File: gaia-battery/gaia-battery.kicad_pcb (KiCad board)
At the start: 2 copper layers, 50 x 50 mm, 3 parts, among them J1 Conn_02x10_Odd_Even, J2 Conn_02x10_Odd_Even, J3 Conn_01x02_Pin

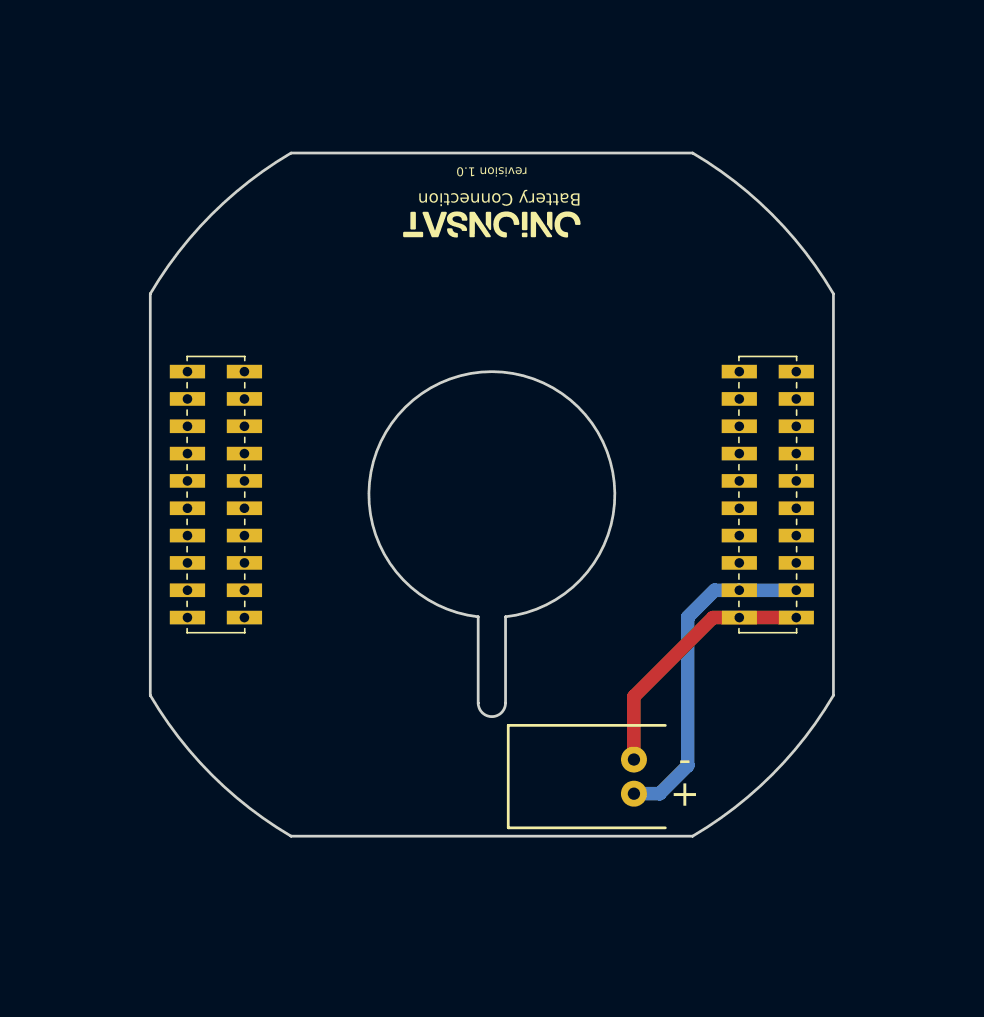
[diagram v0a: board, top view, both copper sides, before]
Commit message: fixing routing problems
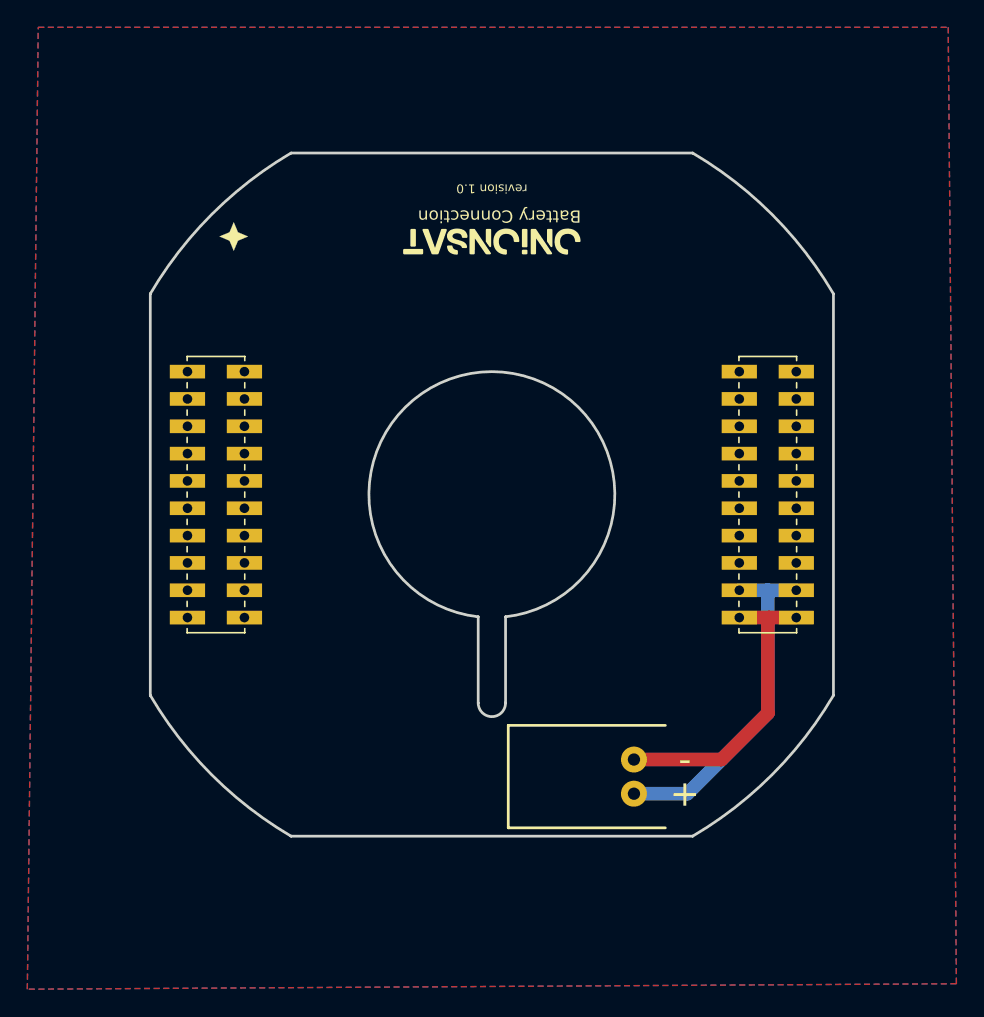
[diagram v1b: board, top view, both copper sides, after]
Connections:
- J1 pad 17: unconnected-(J1-Pin_17-Pad17) -> GND
- J1 pad 18: unconnected-(J1-Pin_18-Pad18) -> GND
- J1 pad 19: unconnected-(J1-Pin_19-Pad19) -> GND
- J1 pad 20: unconnected-(J1-Pin_20-Pad20) -> GND
- J1 pad 7: unconnected-(J1-Pin_7-Pad7) -> GND
- J2 pad 13: unconnected-(J2-Pin_13-Pad13) -> GND
- J2 pad 14: unconnected-(J2-Pin_14-Pad14) -> GND
- J2 pad 15: unconnected-(J2-Pin_15-Pad15) -> GND
- J2 pad 16: unconnected-(J2-Pin_16-Pad16) -> GND
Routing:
- net -BATT: track 18.9 -> 22.4 mm
- net +BATT: track 24.4 -> 25.4 mm
- added copper zone on B.Cu, net GND
- added copper zone on F.Cu, net GND
- added copper zone on In1.Cu, net GND
- added copper zone on In2.Cu, net GND
- added copper zone on In3.Cu, net GND
- added copper zone on In4.Cu, net GND
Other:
- copper layers 2 -> 6

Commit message: update pushing
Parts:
- added REF**: neptune_badge, gaia-battery:neptune_badge_02, F.Cu at (126.5, 115.6)

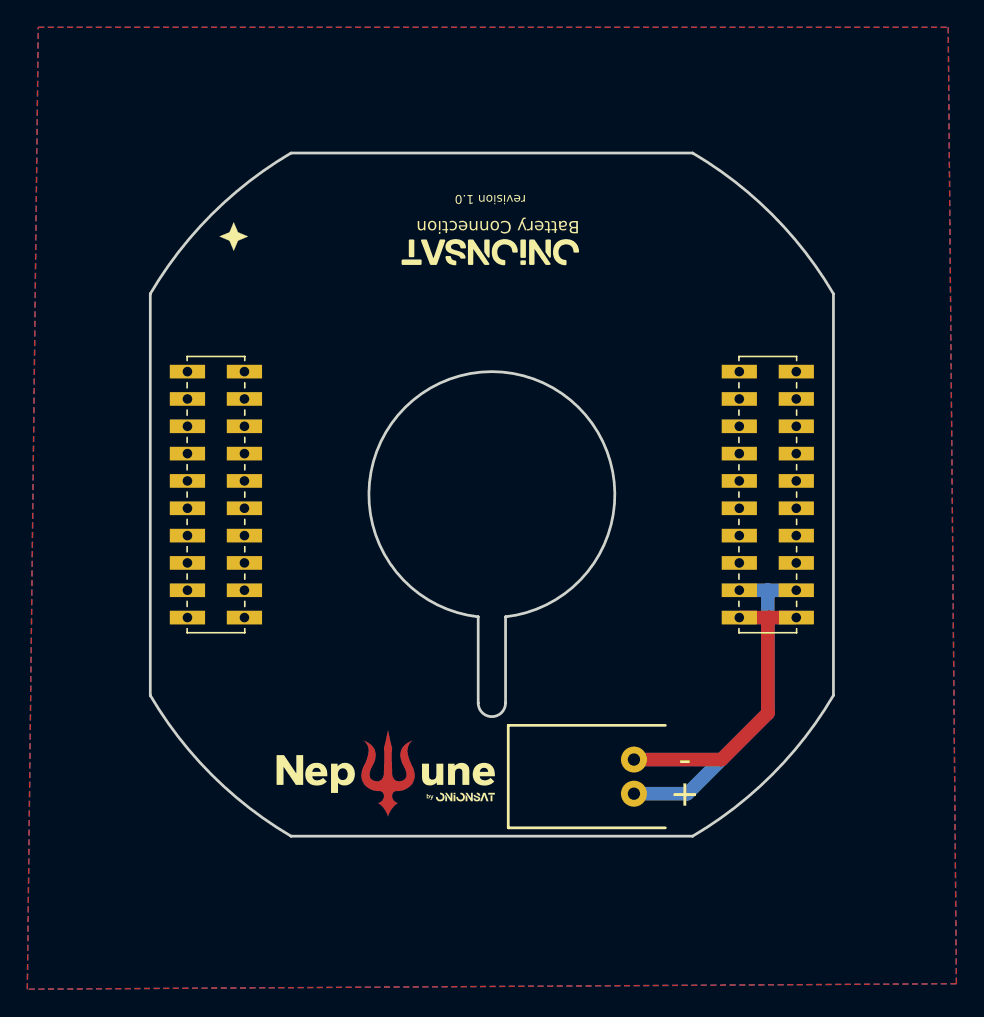
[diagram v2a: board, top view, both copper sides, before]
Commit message: v1.1 - adding rtc battery
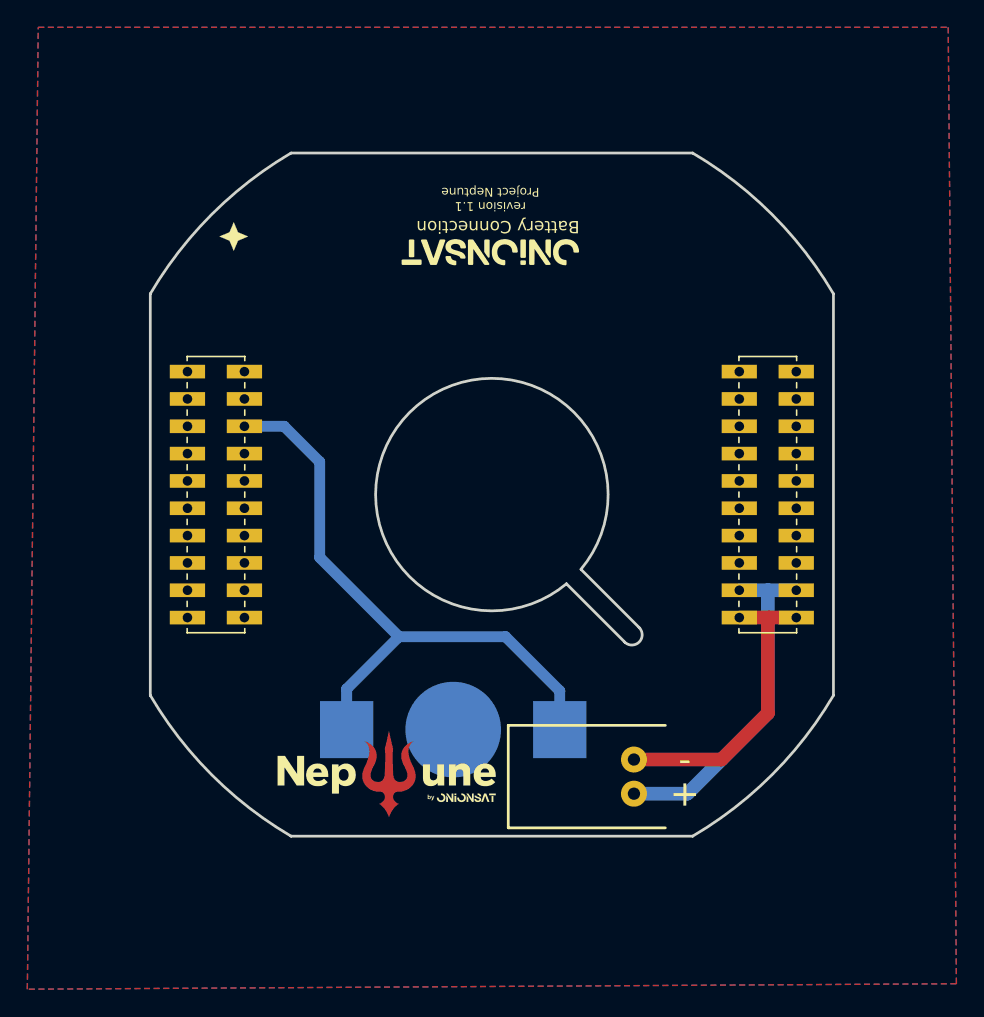
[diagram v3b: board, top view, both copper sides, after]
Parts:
- added BTc1: Battery_Cell, gaia-battery:BAT-SMD_MY-1220-03, B.Cu at (131.3, 112.4)
- moved REF** 0.08 mm to (126.6, 115.6)
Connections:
- J1 pad 10: unconnected-(J1-Pin_10-Pad10) -> GND
- J1 pad 6: unconnected-(J1-Pin_6-Pad6) -> Net-(BTc1-+)
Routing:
- net Net-(BTc1-+): track 0.00 -> 46.4 mm
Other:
- outline, holes or cut-outs redrawn
- board text added: "RTC Battery"
- board text added: "revision 1.1 Project Neptune"
- board text removed: "revision 1.0"

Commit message: v1.1 gnd fix
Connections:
- J1 pad 5: unconnected-(J1-Pin_5-Pad5) -> GND
- J1 pad 9: unconnected-(J1-Pin_9-Pad9) -> GND
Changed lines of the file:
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@@
 	(net 6 "unconnected-(J1-Pin_15-Pad15)")
 	(net 7 "unconnected-(J1-Pin_14-Pad14)")
-	(net 8 "unconnected-(J1-Pin_5-Pad5)")
-	(net 9 "unconnected-(J1-Pin_1-Pad1)")
-	(net 10 "unconnected-(J1-Pin_3-Pad3)")
-	(net 11 "unconnected-(J1-Pin_8-Pad8)")
-	(net 12 "unconnected-(J1-Pin_2-Pad2)")
-	(net 13 "unconnected-(J1-Pin_12-Pad12)")
-	(net 14 "unconnected-(J1-Pin_13-Pad13)")
-	(net 15 "unconnected-(J1-Pin_9-Pad9)")
-	(net 16 "unconnected-(J2-Pin_11-Pad11)")
-	(net 17 "unconnected-(J2-Pin_2-Pad2)")
-	(net 18 "unconnected-(J2-Pin_3-Pad3)")
-	(net 19 "-BATT")
-	(net 20 "unconnected-(J2-Pin_4-Pad4)")
-	(net 21 "unconnected-(J2-Pin_6-Pad6)")
-	(net 22 "unconnected-(J2-Pin_12-Pad12)")
-	(net 23 "+BATT")
-	(net 24 "unconnected-(J2-Pin_8-Pad8)")
-	(net 25 "unconnected-(J2-Pin_5-Pad5)")
-	(net 26 "unconnected-(J2-Pin_10-Pad10)")
-	(net 27 "unconnected-(J2-Pin_9-Pad9)")
-	(net 28 "unconnected-(J2-Pin_1-Pad1)")
-	(net 29 "unconnected-(J2-Pin_7-Pad7)")
+	(net 8 "unconnected-(J1-Pin_1-Pad1)")
+	(net 9 "unconnected-(J1-Pin_3-Pad3)")
+	(net 10 "unconnected-(J1-Pin_8-Pad8)")
+	(net 11 "unconnected-(J1-Pin_2-Pad2)")
+	(net 12 "unconnected-(J1-Pin_12-Pad12)")
+	(net 13 "unconnected-(J1-Pin_13-Pad13)")
+	(net 14 "unconnected-(J2-Pin_11-Pad11)")
+	(net 15 "unconnected-(J2-Pin_2-Pad2)")
+	(net 16 "unconnected-(J2-Pin_3-Pad3)")
+	(net 17 "-BATT")
+	(net 18 "unconnected-(J2-Pin_4-Pad4)")
+	(net 19 "unconnected-(J2-Pin_6-Pad6)")
+	(net 20 "unconnected-(J2-Pin_12-Pad12)")
+	(net 21 "+BATT")
+	(net 22 "unconnected-(J2-Pin_8-Pad8)")
+	(net 23 "unconnected-(J2-Pin_5-Pad5)")
+	(net 24 "unconnected-(J2-Pin_10-Pad10)")
+	(net 25 "unconnected-(J2-Pin_9-Pad9)")
+	(net 26 "unconnected-(J2-Pin_1-Pad1)")
+	(net 27 "unconnected-(J2-Pin_7-Pad7)")
 	(footprint "gaia-battery:Gaia_connector_2_4layer"
 		(layer "F.Cu")
@@
 			(layers "*.Cu" "*.Mask")
 			(remove_unused_layers no)
-			(net 9 "unconnected-(J1-Pin_1-Pad1)")
+			(net 8 "unconnected-(J1-Pin_1-Pad1)")
 			(pinfunction "Pin_1")
 			(pintype "passive+no_connect")
@@
 			(layers "*.Cu" "*.Mask")
 			(remove_unused_layers no)
-			(net 12 "unconnected-(J1-Pin_2-Pad2)")
+			(net 11 "unconnected-(J1-Pin_2-Pad2)")
 			(pinfunction "Pin_2")
 			(pintype "passive+no_connect")
@@
 			(layers "*.Cu" "*.Mask")
 			(remove_unused_layers no)
-			(net 10 "unconnected-(J1-Pin_3-Pad3)")
+			(net 9 "unconnected-(J1-Pin_3-Pad3)")
 			(pinfunction "Pin_3")
 			(pintype "passive+no_connect")
@@
 			(layers "*.Cu" "*.Mask")
 			(remove_unused_layers no)
-			(net 8 "unconnected-(J1-Pin_5-Pad5)")
+			(net 4 "GND")
 			(pinfunction "Pin_5")
-			(pintype "passive+no_connect")
+			(pintype "passive")
 		)
 		(pad "6" thru_hole rect
@@
 			(layers "*.Cu" "*.Mask")
 			(remove_unused_layers no)
-			(net 11 "unconnected-(J1-Pin_8-Pad8)")
+			(net 10 "unconnected-(J1-Pin_8-Pad8)")
 			(pinfunction "Pin_8")
 			(pintype "passive+no_connect")
@@
 			(layers "*.Cu" "*.Mask")
 			(remove_unused_layers no)
-			(net 15 "unconnected-(J1-Pin_9-Pad9)")
+			(net 4 "GND")
 			(pinfunction "Pin_9")
 			(pintype "passive")
@@
 			(layers "*.Cu" "*.Mask")
 			(remove_unused_layers no)
-			(net 13 "unconnected-(J1-Pin_12-Pad12)")
+			(net 12 "unconnected-(J1-Pin_12-Pad12)")
 			(pinfunction "Pin_12")
 			(pintype "passive+no_connect")
@@
 			(layers "*.Cu" "*.Mask")
 			(remove_unused_layers no)
-			(net 14 "unconnected-(J1-Pin_13-Pad13)")
+			(net 13 "unconnected-(J1-Pin_13-Pad13)")
 			(pinfunction "Pin_13")
 			(pintype "passive+no_connect")
@@
 			(layers "*.Cu" "*.Mask")
 			(remove_unused_layers no)
-			(net 23 "+BATT")
+			(net 21 "+BATT")
 			(pinfunction "Pin_1")
 			(pintype "passive")
@@
 			(layers "*.Cu" "*.Mask")
 			(remove_unused_layers no)
-			(net 19 "-BATT")
+			(net 17 "-BATT")
 			(pinfunction "Pin_2")
 			(pintype "passive")
@@
 			(layers "*.Cu" "*.Mask")
 			(remove_unused_layers no)
-			(net 28 "unconnected-(J2-Pin_1-Pad1)")
+			(net 26 "unconnected-(J2-Pin_1-Pad1)")
 			(pinfunction "Pin_1")
 			(pintype "passive+no_connect")
@@
 			(layers "*.Cu" "*.Mask")
 			(remove_unused_layers no)
-			(net 17 "unconnected-(J2-Pin_2-Pad2)")
+			(net 15 "unconnected-(J2-Pin_2-Pad2)")
 			(pinfunction "Pin_2")
 			(pintype "passive+no_connect")
@@
 			(layers "*.Cu" "*.Mask")
 			(remove_unused_layers no)
-			(net 18 "unconnected-(J2-Pin_3-Pad3)")
+			(net 16 "unconnected-(J2-Pin_3-Pad3)")
 			(pinfunction "Pin_3")
 			(pintype "passive+no_connect")
@@
 			(layers "*.Cu" "*.Mask")
 			(remove_unused_layers no)
-			(net 20 "unconnected-(J2-Pin_4-Pad4)")
+			(net 18 "unconnected-(J2-Pin_4-Pad4)")
 			(pinfunction "Pin_4")
 			(pintype "passive+no_connect")
@@
 			(layers "*.Cu" "*.Mask")
 			(remove_unused_layers no)
-			(net 25 "unconnected-(J2-Pin_5-Pad5)")
+			(net 23 "unconnected-(J2-Pin_5-Pad5)")
 			(pinfunction "Pin_5")
 			(pintype "passive+no_connect")
@@
 			(layers "*.Cu" "*.Mask")
 			(remove_unused_layers no)
-			(net 21 "unconnected-(J2-Pin_6-Pad6)")
+			(net 19 "unconnected-(J2-Pin_6-Pad6)")
 			(pinfunction "Pin_6")
 			(pintype "passive+no_connect")
@@
 			(layers "*.Cu" "*.Mask")
 			(remove_unused_layers no)
-			(net 29 "unconnected-(J2-Pin_7-Pad7)")
+			(net 27 "unconnected-(J2-Pin_7-Pad7)")
 			(pinfunction "Pin_7")
 			(pintype "passive+no_connect")
@@
 			(layers "*.Cu" "*.Mask")
 			(remove_unused_layers no)
-			(net 24 "unconnected-(J2-Pin_8-Pad8)")
+			(net 22 "unconnected-(J2-Pin_8-Pad8)")
 			(pinfunction "Pin_8")
 			(pintype "passive+no_connect")
@@
 			(layers "*.Cu" "*.Mask")
 			(remove_unused_layers no)
-			(net 27 "unconnected-(J2-Pin_9-Pad9)")
+			(net 25 "unconnected-(J2-Pin_9-Pad9)")
 			(pinfunction "Pin_9")
 			(pintype "passive+no_connect")
@@
 			(layers "*.Cu" "*.Mask")
 			(remove_unused_layers no)
-			(net 26 "unconnected-(J2-Pin_10-Pad10)")
+			(net 24 "unconnected-(J2-Pin_10-Pad10)")
 			(pinfunction "Pin_10")
 			(pintype "passive+no_connect")
@@
 			(layers "*.Cu" "*.Mask")
 			(remove_unused_layers no)
-			(net 16 "unconnected-(J2-Pin_11-Pad11)")
+			(net 14 "unconnected-(J2-Pin_11-Pad11)")
 			(pinfunction "Pin_11")
 			(pintype "passive+no_connect")
@@
 			(layers "*.Cu" "*.Mask")
 			(remove_unused_layers no)
-			(net 22 "unconnected-(J2-Pin_12-Pad12)")
+			(net 20 "unconnected-(J2-Pin_12-Pad12)")
 			(pinfunction "Pin_12")
 			(pintype "passive+no_connect")
@@
 			(layers "*.Cu" "*.Mask")
 			(remove_unused_layers no)
-			(net 23 "+BATT")
+			(net 21 "+BATT")
 			(pinfunction "Pin_17")
 			(pintype "passive")
@@
 			(layers "*.Cu" "*.Mask")
 			(remove_unused_layers no)
-			(net 23 "+BATT")
+			(net 21 "+BATT")
 			(pinfunction "Pin_18")
 			(pintype "passive")
@@
 			(layers "*.Cu" "*.Mask")
 			(remove_unused_layers no)
-			(net 19 "-BATT")
+			(net 17 "-BATT")
 			(pinfunction "Pin_19")
 			(pintype "passive")
@@
 			(layers "*.Cu" "*.Mask")
 			(remove_unused_layers no)
-			(net 19 "-BATT")
+			(net 17 "-BATT")
 			(pinfunction "Pin_20")
 			(pintype "passive")
@@
 		(width 1)
 		(layer "F.Cu")
-		(net 19)
+		(net 17)
 	)
 	(segment
@@
 		(width 1)
 		(layer "F.Cu")
-		(net 19)
+		(net 17)
 	)
 	(segment
@@
 		(width 1)
 		(layer "F.Cu")
-		(net 19)
+		(net 17)
 	)
 	(segment
@@
 		(width 1)
 		(layer "F.Cu")
-		(net 19)
+		(net 17)
 	)
 	(segment
@@
 		(width 1)
 		(layer "F.Cu")
-		(net 19)
+		(net 17)
 	)
 	(segment
@@
 		(width 1)
 		(layer "F.Cu")
-		(net 19)
+		(net 17)
 	)
 	(segment
@@
 		(width 1)
 		(layer "B.Cu")
-		(net 23)
+		(net 21)
 	)
 	(segment
@@
 		(width 1)
 		(layer "B.Cu")
-		(net 23)
+		(net 21)
 	)
 	(segment
@@
 		(width 1)
 		(layer "B.Cu")
-		(net 23)
+		(net 21)
 	)
 	(segment
@@
 		(width 1)
 		(layer "B.Cu")
-		(net 23)
+		(net 21)
 	)
 	(segment
@@
 		(width 1)
 		(layer "B.Cu")
-		(net 23)
+		(net 21)
 	)
 	(zone
